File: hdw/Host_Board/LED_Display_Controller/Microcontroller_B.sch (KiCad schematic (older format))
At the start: 1 part

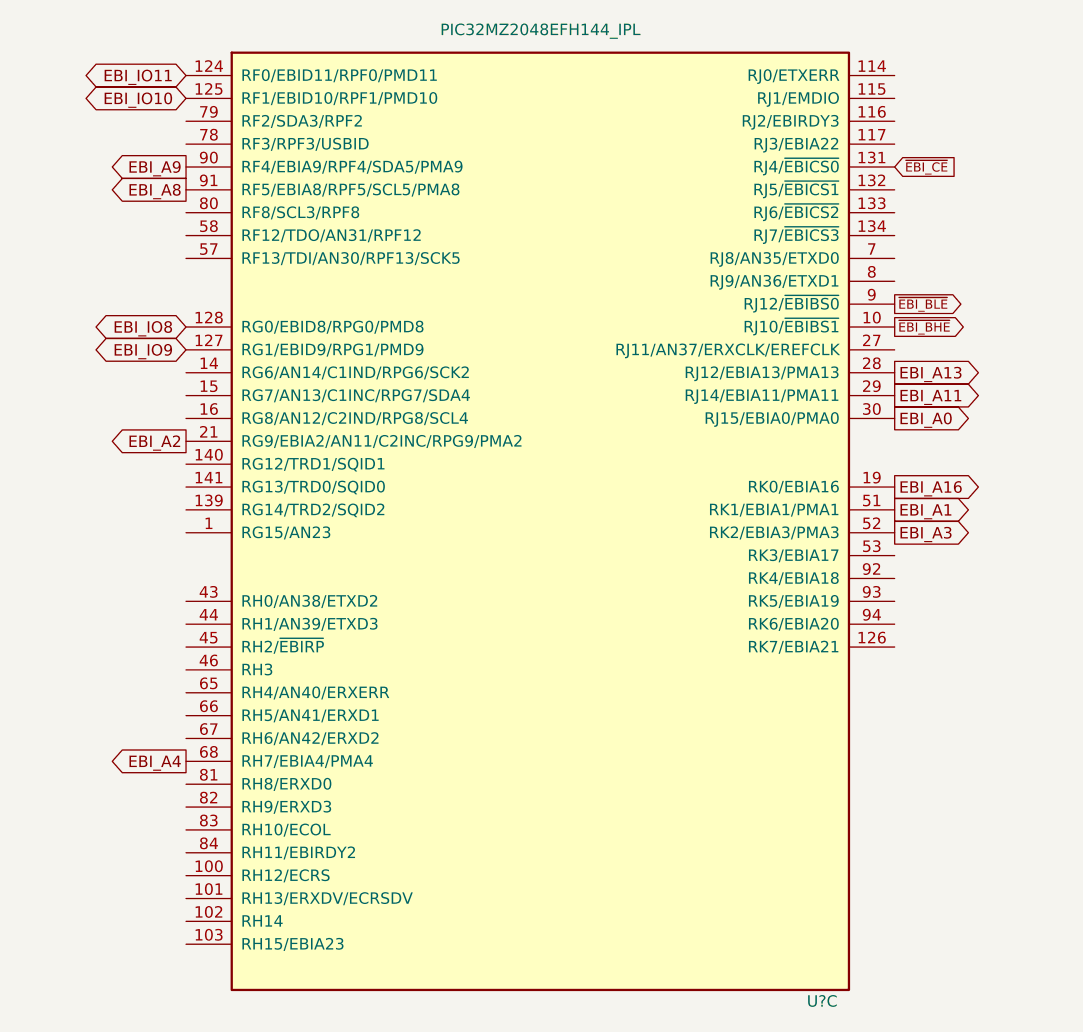
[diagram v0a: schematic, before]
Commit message: Connected new external SRAM to micro
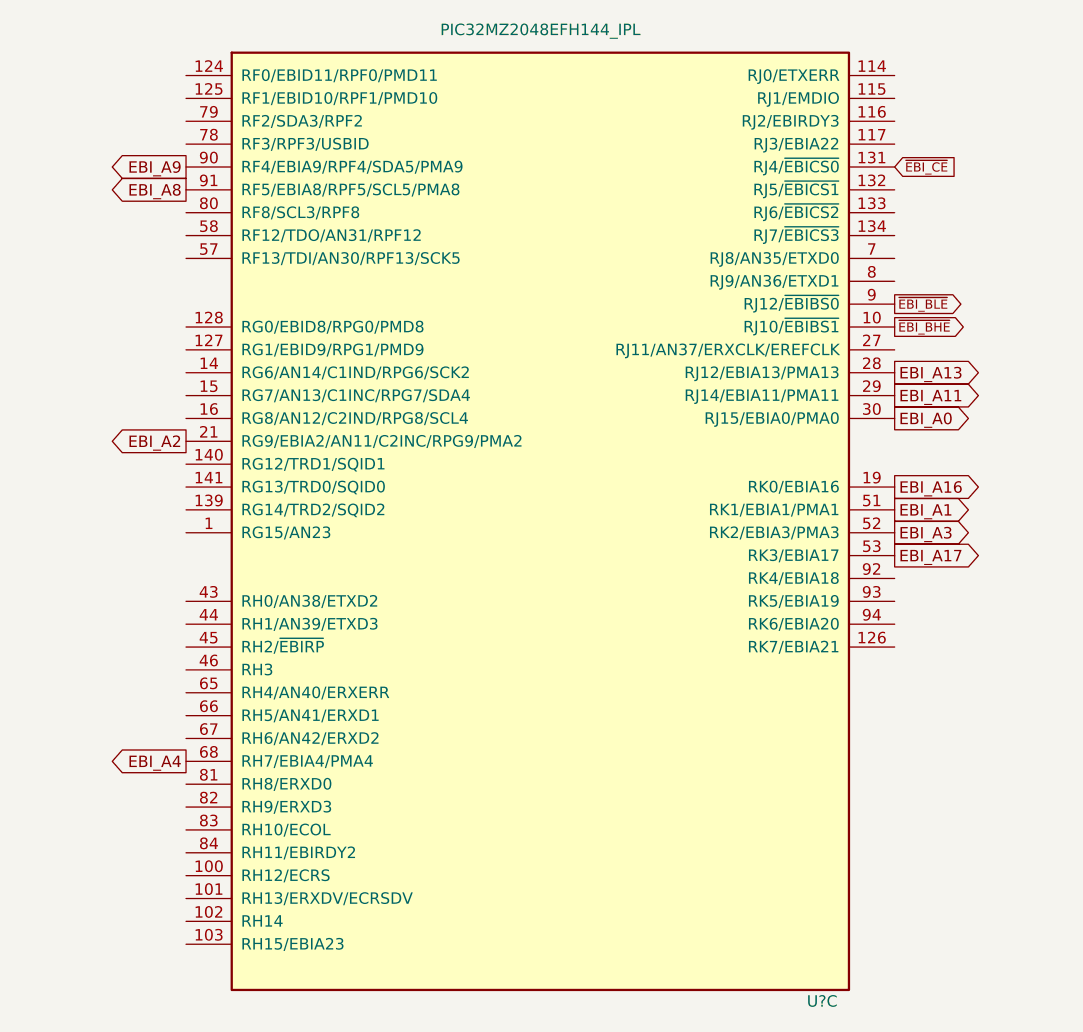
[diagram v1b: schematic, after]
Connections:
- net EBI_A17: now reaches U?.53 (RK3/EBIA17)
- net EBI_IO10: no longer names the net of U?.125 (RF1/EBID10/RPF1/PMD10)
- net EBI_IO11: no longer names the net of U?.124 (RF0/EBID11/RPF0/PMD11)
- net EBI_IO8: no longer names the net of U?.128 (RG0/EBID8/RPG0/PMD8)
- net EBI_IO9: no longer names the net of U?.127 (RG1/EBID9/RPG1/PMD9)
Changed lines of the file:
@@
 Text GLabel 7130 1980 2    40   Input ~ 0
 ~EBI_CE
-Text GLabel 4030 2680 0    50   BiDi ~ 0
-EBI_IO8
-Text GLabel 4030 2780 0    50   BiDi ~ 0
-EBI_IO9
-Text GLabel 4030 1680 0    50   BiDi ~ 0
-EBI_IO10
-Text GLabel 4030 1580 0    50   BiDi ~ 0
-EBI_IO11
+Text GLabel 7130 3680 2    50   Output ~ 0
+EBI_A17
 $EndSCHEMATC

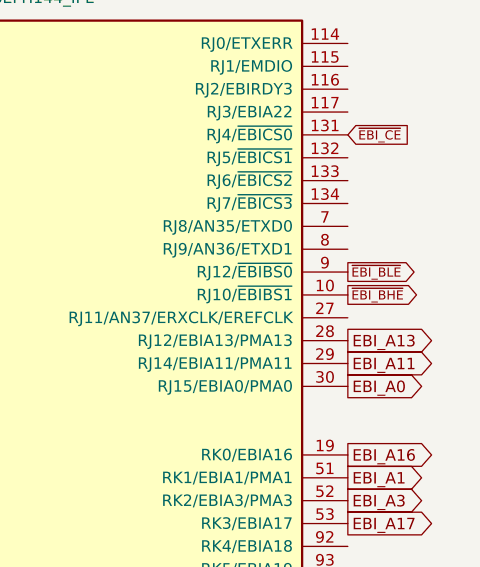
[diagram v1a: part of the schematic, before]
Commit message: Removed unneeded EBI nets
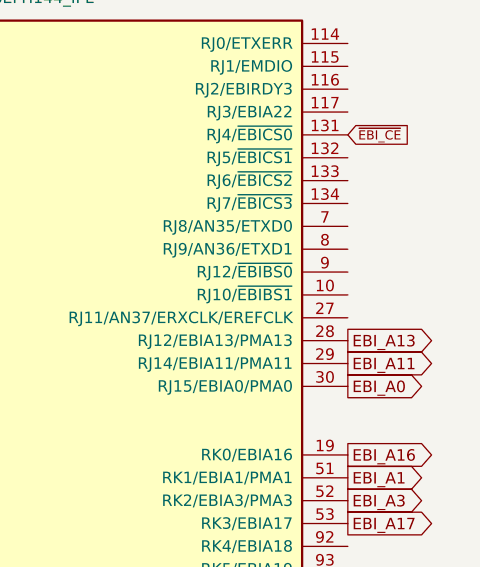
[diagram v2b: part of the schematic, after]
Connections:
- net ~EBI_BHE: no longer names the net of U?.10 (RJ10/~EBIBS1~)
- net ~EBI_BLE: no longer names the net of U?.9 (RJ12/~EBIBS0~)
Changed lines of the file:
@@
 Text GLabel 7130 3380 2    50   Output ~ 0
 EBI_A16
-Text GLabel 7130 2680 2    40   Output ~ 0
-~EBI_BHE
-Text GLabel 7130 2580 2    40   Output ~ 0
-~EBI_BLE
 Text GLabel 7130 1980 2    40   Input ~ 0
 ~EBI_CE

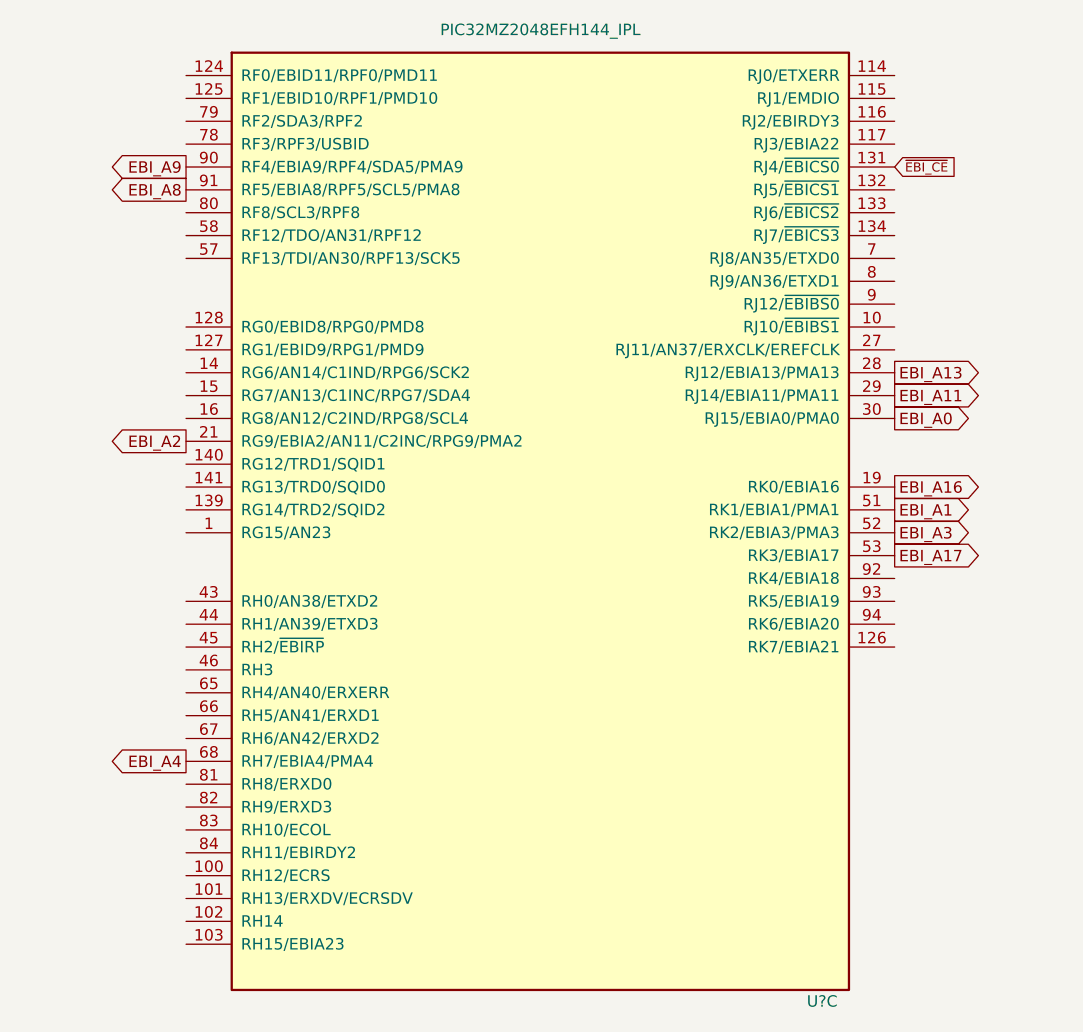
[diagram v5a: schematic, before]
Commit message: connected signals to MCU pins
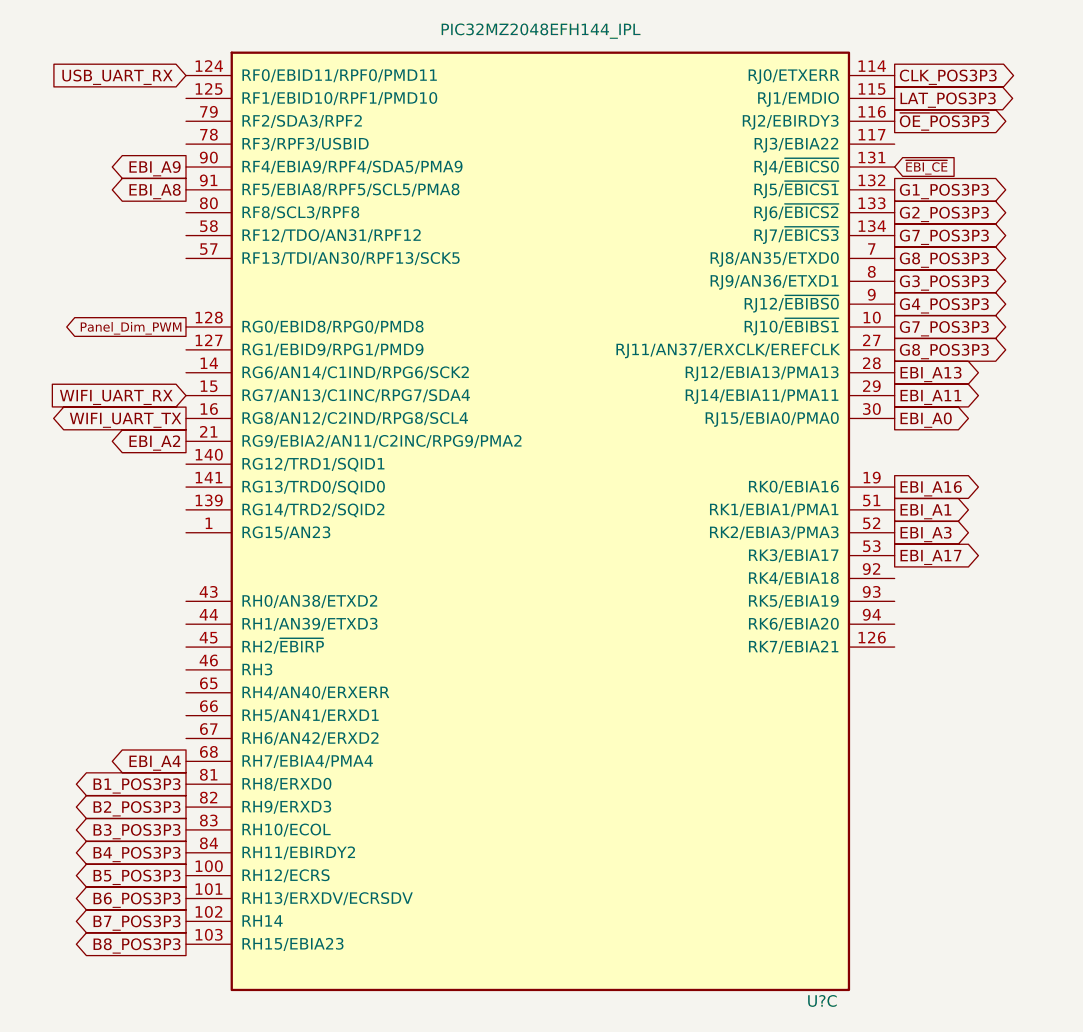
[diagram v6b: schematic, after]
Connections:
- net G7_POS3P3: now reaches U?.10 (RJ10/~EBIBS1~)
- net G7_POS3P3: now also U?.134 (RJ7/~EBICS3~)
- net B5_POS3P3: now reaches U?.100 (RH12/ECRS)
- net B6_POS3P3: now reaches U?.101 (RH13/ERXDV/ECRSDV)
- net B7_POS3P3: now reaches U?.102 (RH14)
- net B8_POS3P3: now reaches U?.103 (RH15/EBIA23)
- net CLK_POS3P3: now reaches U?.114 (RJ0/ETXERR)
- net LAT_POS3P3: now reaches U?.115 (RJ1/EMDIO)
- net ~OE_POS3P3: now reaches U?.116 (RJ2/EBIRDY3)
- net USB_UART_RX: now reaches U?.124 (RF0/EBID11/RPF0/PMD11)
- net Panel_Dim_PWM: now reaches U?.128 (RG0/EBID8/RPG0/PMD8)
- net G1_POS3P3: now reaches U?.132 (RJ5/~EBICS1~)
- net G2_POS3P3: now reaches U?.133 (RJ6/~EBICS2~)
- net WIFI_UART_RX: now reaches U?.15 (RG7/AN13/C1INC/RPG7/SDA4)
- net WIFI_UART_TX: now reaches U?.16 (RG8/AN12/C2IND/RPG8/SCL4)
- net G8_POS3P3: now reaches U?.27 (RJ11/AN37/ERXCLK/EREFCLK)
- net G8_POS3P3: now also U?.7 (RJ8/AN35/ETXD0)
- net G3_POS3P3: now reaches U?.8 (RJ9/AN36/ETXD1)
- net B1_POS3P3: now reaches U?.81 (RH8/ERXD0)
- net B2_POS3P3: now reaches U?.82 (RH9/ERXD3)
- net B3_POS3P3: now reaches U?.83 (RH10/ECOL)
- net B4_POS3P3: now reaches U?.84 (RH11/EBIRDY2)
- net G4_POS3P3: now reaches U?.9 (RJ12/~EBIBS0~)
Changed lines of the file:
@@
 $Descr A 11000 8500
 encoding utf-8
-Sheet 12 30
+Sheet 11 30
 Title ""
 Date ""
@@
 Text GLabel 7130 3680 2    50   Output ~ 0
 EBI_A17
+Text GLabel 7130 2080 2    50   Output ~ 0
+G1_POS3P3
+Text GLabel 7130 2180 2    50   Output ~ 0
+G2_POS3P3
+Text GLabel 7130 2480 2    50   Output ~ 0
+G3_POS3P3
+Text GLabel 7130 2580 2    50   Output ~ 0
+G4_POS3P3
+Text GLabel 7130 2280 2    50   Output ~ 0
+G7_POS3P3
+Text GLabel 7130 2380 2    50   Output ~ 0
+G8_POS3P3
+Text GLabel 7130 2680 2    50   Output ~ 0
+G7_POS3P3
+Text GLabel 7130 2780 2    50   Output ~ 0
+G8_POS3P3
+Text GLabel 4030 4680 0    50   Output ~ 0
+B1_POS3P3
+Text GLabel 4030 4780 0    50   Output ~ 0
+B2_POS3P3
+Text GLabel 4030 4880 0    50   Output ~ 0
+B3_POS3P3
+Text GLabel 4030 4980 0    50   Output ~ 0
+B4_POS3P3
+Text GLabel 4030 5080 0    50   Output ~ 0
+B5_POS3P3
+Text GLabel 4030 5180 0    50   Output ~ 0
+B6_POS3P3
+Text GLabel 4030 5280 0    50   Output ~ 0
+B7_POS3P3
+Text GLabel 4030 5380 0    50   Output ~ 0
+B8_POS3P3
+Text GLabel 4030 1580 0    50   Input ~ 0
+USB_UART_RX
+Text GLabel 4030 3080 0    50   Output ~ 0
+WIFI_UART_TX
+Text GLabel 4030 2980 0    50   Input ~ 0
+WIFI_UART_RX
+Text GLabel 7130 1580 2    50   Output ~ 0
+CLK_POS3P3
+Text GLabel 7130 1680 2    50   Output ~ 0
+LAT_POS3P3
+Text GLabel 7130 1780 2    50   Output ~ 0
+~OE_POS3P3
+Text GLabel 4030 2680 0    40   Output ~ 0
+Panel_Dim_PWM
 $EndSCHEMATC
